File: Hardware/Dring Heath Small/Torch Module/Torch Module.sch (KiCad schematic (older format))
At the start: 32 parts, among them J1 Torch, J2 Module3, J3 Conn_01x18_Male, J4 Limit, J6 Motor, J7 Module1, K1 G6E, Q1 AO3400A, U1 ULN2002

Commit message: Main and Module Boards Routed
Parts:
- removed C3: 1uf, Capacitor_SMD:C_0603_1608Metric_Pad1.08x0.95mm_HandSolder, symbol Device:C_Small
- removed R10: 3.3k, Resistor_SMD:R_0603_1608Metric_Pad0.98x0.95mm_HandSolder, symbol Device:R_US
- removed R8: 10k, Resistor_SMD:R_0603_1608Metric_Pad0.98x0.95mm_HandSolder, symbol Device:R_US
- removed R9: 1k, Resistor_SMD:R_0603_1608Metric_Pad0.98x0.95mm_HandSolder, symbol Device:R_US
- added J10: Module conn, Connector_PinHeader_2.54mm:PinHeader_1x12_P2.54mm_Vertical, symbol Connector:Conn_01x12_Male
- added J8: 2.54 pin, Connector_PinHeader_2.54mm:PinHeader_2x05_P2.54mm_Vertical, symbol Connector:Conn_01x10_Male
- added J9: 1.27 pin, Connector_PinHeader_1.27mm:PinHeader_2x05_P1.27mm_Vertical, symbol Connector:Conn_01x10_Male
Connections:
- net at U1.13 (O4): now also J3.11 (Pin_11)
- net at U1.5 (I5), U1.6 (I6), U1.7 (I7)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: now also J3.15 (Pin_15), J3.9 (Pin_9); no longer U1.4 (I4)
- net at J3.17 (Pin_17): no longer J3.18 (Pin_18)
- net at J3.4 (Pin_4): now also U1.4 (I4)
- new net: J10.1 (Pin_1), J8.3 (Pin_3), J8.5 (Pin_5), J8.9 (Pin_9), J9.3 (Pin_3), J9.5 (Pin_5), J9.9 (Pin_9)
- new net: J10.10 (Pin_10), J8.6 (Pin_6), J9.6 (Pin_6)
- new net: J10.11 (Pin_11), J8.8 (Pin_8), J9.8 (Pin_8)
- new net: J10.3 (Pin_3), J8.1 (Pin_1), J9.1 (Pin_1)
- new net: J10.8 (Pin_8), J8.2 (Pin_2), J9.2 (Pin_2)
- new net: J10.9 (Pin_9), J8.4 (Pin_4), J9.4 (Pin_4)
- no-connect marks 29 -> 37
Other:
- note added: "Jtag"
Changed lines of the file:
@@
 NoConn ~ 3200 3000
 NoConn ~ 3900 3600
-$Comp
-L Transistor_Array:ULN2002 U1
-U 1 1 5FF8EFB7
-P 4100 4950
-F 0 "U1" H 4250 5600 50  0000 C CNN
-F 1 "ULN2002" H 4250 5500 50  0000 C CNN
-F 2 "Package_SO:SO-16_3.9x9.9mm_P1.27mm" H 4150 4400 50  0001 L CNN
-F 3 "http://www.ti.com/lit/ds/symlink/uln2003a.pdf" H 4200 4750 50  0001 C CNN
-	1    4100 4950
-	1    0    0    -1
-$EndComp
-$Comp
-L Device:C_Small C3
-U 1 1 5FF90392
-P 5050 5450
-AR Path="/5FF90392" Ref="C3"  Part="1"
-AR Path="/61469ABE/5FF90392" Ref="C?"  Part="1"
-F 0 "C3" H 4958 5404 50  0000 R CNN
-F 1 "1uf" H 4958 5495 50  0000 R CNN
-F 2 "Capacitor_SMD:C_0603_1608Metric_Pad1.08x0.95mm_HandSolder" H 5050 5450 50  0001 C CNN
-F 3 "~" H 5050 5450 50  0001 C CNN
-	1    5050 5450
-	-1   0    0    1
-$EndComp
-$Comp
-L Device:R_US R8
-U 1 1 5FF9039C
-P 4900 5200
-AR Path="/5FF9039C" Ref="R8"  Part="1"
-AR Path="/61469ABE/5FF9039C" Ref="R?"  Part="1"
-F 0 "R8" V 4700 5300 50  0000 C CNN
-F 1 "10k" V 4800 5250 50  0000 C CNN
-F 2 "Resistor_SMD:R_0603_1608Metric_Pad0.98x0.95mm_HandSolder" V 4940 5190 50  0001 C CNN
-F 3 "~" H 4900 5200 50  0001 C CNN
-	1    4900 5200
-	0    1    1    0
-$EndComp
-$Comp
-L Device:R_US R9
-U 1 1 5FF903A6
-P 4750 5350
-AR Path="/5FF903A6" Ref="R9"  Part="1"
-AR Path="/61469ABE/5FF903A6" Ref="R?"  Part="1"
-F 0 "R9" H 4600 5400 50  0000 L CNN
-F 1 "1k" H 4600 5300 50  0000 L CNN
-F 2 "Resistor_SMD:R_0603_1608Metric_Pad0.98x0.95mm_HandSolder" V 4790 5340 50  0001 C CNN
-F 3 "~" H 4750 5350 50  0001 C CNN
-	1    4750 5350
-	-1   0    0    1
-$EndComp
-$Comp
-L Device:R_US R10
-U 1 1 5FF903B0
-P 4750 5050
-AR Path="/5FF903B0" Ref="R10"  Part="1"
-AR Path="/61469ABE/5FF903B0" Ref="R?"  Part="1"
-F 0 "R10" V 4950 5150 50  0000 R CNN
-F 1 "3.3k" V 4850 5150 50  0000 R CNN
-F 2 "Resistor_SMD:R_0603_1608Metric_Pad0.98x0.95mm_HandSolder" V 4790 5040 50  0001 C CNN
-F 3 "~" H 4750 5050 50  0001 C CNN
-	1    4750 5050
-	-1   0    0    -1
-$EndComp
-Wire Wire Line
-	5050 5350 5050 5200
-Wire Wire Line
-	4100 5550 4750 5550
-Wire Wire Line
-	4750 5550 4750 5500
-Wire Wire Line
-	4750 5550 5050 5550
-Connection ~ 4750 5550
 NoConn ~ 4500 5350
 NoConn ~ 4500 5250
 NoConn ~ 4500 5150
-NoConn ~ 4500 5050
 Wire Wire Line
 	5750 3500 5250 3500
@@
 Wire Wire Line
 	3450 4750 3700 4750
-Connection ~ 4750 5200
 Wire Wire Line
 	4500 4550 4950 4550
@@
 	3600 4850 3700 4850
 Wire Wire Line
-	5050 5200 5050 4150
-Connection ~ 5050 5200
-Wire Wire Line
-	5150 4150 5050 4150
-Connection ~ 5050 4150
-Wire Wire Line
-	4450 4150 4450 4300
-Wire Wire Line
-	4450 4300 4850 4300
-Wire Wire Line
-	4850 4300 4850 4900
-Wire Wire Line
-	4850 4900 4750 4900
-Wire Wire Line
-	3700 5050 3700 5150
-Wire Wire Line
-	3700 5150 3700 5250
-Connection ~ 3700 5150
-Wire Wire Line
-	3700 5250 3700 5350
-Connection ~ 3700 5250
-Wire Wire Line
-	3700 5350 3700 5550
-Wire Wire Line
 	3700 5550 4100 5550
-Connection ~ 3700 5350
-Connection ~ 4100 5550
 Wire Wire Line
 	4500 4950 4550 4950
 Wire Wire Line
 	4550 4950 4550 4150
-NoConn ~ 4850 4150
 NoConn ~ 4350 4150
-NoConn ~ 4250 4150
 NoConn ~ 3950 4150
 NoConn ~ 3850 4150
-NoConn ~ 3750 4150
 NoConn ~ 3650 4150
 NoConn ~ 3550 4150
@@
 	-1   0    0    1
 $EndComp
+$Comp
+L Connector:Conn_01x12_Male J?
+U 1 1 600F49D0
+P 5200 6600
+AR Path="/61469ABE/600F49D0" Ref="J?"  Part="1"
+AR Path="/600F49D0" Ref="J10"  Part="1"
+F 0 "J10" H 5150 7050 50  0000 R CNN
+F 1 "Module conn" V 5100 6700 50  0000 R CNN
+F 2 "Connector_PinHeader_2.54mm:PinHeader_1x12_P2.54mm_Vertical" H 5200 6600 50  0001 C CNN
+F 3 "~" H 5200 6600 50  0001 C CNN
+	1    5200 6600
+	-1   0    0    -1
+$EndComp
+$Comp
+L Connector:Conn_01x10_Male J9
+U 1 1 600FA13A
+P 4000 6600
+F 0 "J9" H 4108 7181 50  0000 C CNN
+F 1 "1.27 pin" H 4108 7090 50  0000 C CNN
+F 2 "Connector_PinHeader_1.27mm:PinHeader_2x05_P1.27mm_Vertical" H 4000 6600 50  0001 C CNN
+F 3 "~" H 4000 6600 50  0001 C CNN
+	1    4000 6600
+	1    0    0    -1
+$EndComp
+$Comp
+L Connector:Conn_01x10_Male J8
+U 1 1 600FD9D8
+P 3450 6600
+F 0 "J8" H 3558 7181 50  0000 C CNN
+F 1 "2.54 pin" H 3558 7090 50  0000 C CNN
+F 2 "Connector_PinHeader_2.54mm:PinHeader_2x05_P2.54mm_Vertical" H 3450 6600 50  0001 C CNN
+F 3 "~" H 3450 6600 50  0001 C CNN
+	1    3450 6600
+	1    0    0    -1
+$EndComp
+Wire Wire Line
+	4200 6300 4750 6300
+Wire Wire Line
+	4750 6300 4750 6800
+Wire Wire Line
+	4750 6800 5000 6800
+Wire Wire Line
+	4200 6500 4700 6500
+Wire Wire Line
+	4700 6500 4700 6900
+Wire Wire Line
+	4700 6900 5000 6900
+Wire Wire Line
+	4200 6700 4650 6700
+Wire Wire Line
+	4650 6700 4650 7000
+Wire Wire Line
+	4650 7000 5000 7000
+Wire Wire Line
+	4200 6900 4600 6900
+Wire Wire Line
+	4600 6900 4600 7100
+Wire Wire Line
+	4600 7100 5000 7100
+Wire Wire Line
+	4850 6300 5000 6300
+Wire Wire Line
+	4200 7000 4400 7000
+Wire Wire Line
+	4400 7000 4400 6600
+Wire Wire Line
+	4200 6600 4400 6600
+Wire Wire Line
+	4200 6200 4850 6200
+Wire Wire Line
+	4850 6200 4850 6300
+Wire Wire Line
+	4200 6400 4400 6400
+Wire Wire Line
+	4400 6400 4400 6600
+Connection ~ 4400 6600
+Wire Wire Line
+	4400 6400 4400 6100
+Wire Wire Line
+	4400 6100 5000 6100
+Connection ~ 4400 6400
+Wire Wire Line
+	3650 6200 3650 6250
+Wire Wire Line
+	3650 6250 4200 6250
+Wire Wire Line
+	4200 6250 4200 6200
+Connection ~ 4200 6200
+Wire Wire Line
+	3650 6300 3650 6350
+Wire Wire Line
+	3650 6350 4200 6350
+Wire Wire Line
+	4200 6350 4200 6300
+Connection ~ 4200 6300
+Wire Wire Line
+	3650 6400 3650 6450
+Wire Wire Line
+	3650 6450 4200 6450
+Wire Wire Line
+	4200 6450 4200 6400
+Connection ~ 4200 6400
+Wire Wire Line
+	3650 6500 3650 6550
+Wire Wire Line
+	3650 6550 4200 6550
+Wire Wire Line
+	4200 6550 4200 6500
+Connection ~ 4200 6500
+Wire Wire Line
+	3650 6600 3650 6650
+Wire Wire Line
+	3650 6650 4200 6650
+Wire Wire Line
+	4200 6650 4200 6600
+Connection ~ 4200 6600
+Wire Wire Line
+	3650 6700 3650 6750
+Wire Wire Line
+	3650 6900 3650 6950
+Wire Wire Line
+	3650 6950 4200 6950
+Wire Wire Line
+	4200 6950 4200 6900
+Connection ~ 4200 6900
+Wire Wire Line
+	3650 7000 3650 7050
+Wire Wire Line
+	3650 7050 4200 7050
+Wire Wire Line
+	4200 7050 4200 7000
+Connection ~ 4200 7000
+Wire Notes Line
+	3300 5900 5500 5900
+Wire Notes Line
+	5500 5900 5500 7450
+Wire Notes Line
+	5500 7450 3300 7450
+Wire Notes Line
+	3300 7450 3300 5900
+Text Notes 3400 7400 0    118  ~ 24
+Jtag
+NoConn ~ 5000 6200
+NoConn ~ 5000 6400
+NoConn ~ 5000 6500
+NoConn ~ 5000 6600
+NoConn ~ 5000 6700
+NoConn ~ 5000 7200
+Wire Wire Line
+	3650 6750 4200 6750
+Wire Wire Line
+	4200 6750 4200 6700
+Connection ~ 4200 6700
+NoConn ~ 3650 6800
+NoConn ~ 3650 7100
+NoConn ~ 4200 7100
+NoConn ~ 4200 6800
+NoConn ~ 5150 4150
+NoConn ~ 5050 4150
+Wire Wire Line
+	3750 4150 3750 4250
+Wire Wire Line
+	3750 4250 3500 4250
+Wire Wire Line
+	3500 4250 3500 5050
+Wire Wire Line
+	3500 5050 3700 5050
+Wire Wire Line
+	3700 5350 3700 5550
+Connection ~ 3700 5350
+Wire Wire Line
+	3700 5250 3700 5350
+Wire Wire Line
+	3700 5150 3700 5250
+Connection ~ 3700 5250
+$Comp
+L Transistor_Array:ULN2002 U1
+U 1 1 5FF8EFB7
+P 4100 4950
+F 0 "U1" H 4250 5600 50  0000 C CNN
+F 1 "ULN2002" H 4250 5500 50  0000 C CNN
+F 2 "Package_SO:SO-16_3.9x9.9mm_P1.27mm" H 4150 4400 50  0001 L CNN
+F 3 "http://www.ti.com/lit/ds/symlink/uln2003a.pdf" H 4200 4750 50  0001 C CNN
+	1    4100 4950
+	1    0    0    -1
+$EndComp
+Wire Wire Line
+	4500 5050 4850 5050
+Wire Wire Line
+	4850 5050 4850 4300
+Wire Wire Line
+	4850 4300 4450 4300
+Wire Wire Line
+	4450 4300 4450 4150
+Wire Wire Line
+	4250 4150 4250 4200
+Wire Wire Line
+	4250 4200 4850 4200
+Wire Wire Line
+	4850 4200 4850 4150
+Wire Wire Line
+	4850 4200 5000 4200
+Wire Wire Line
+	5000 4200 5000 5550
+Wire Wire Line
+	5000 5550 4100 5550
+Connection ~ 4850 4200
+Connection ~ 4100 5550
 $EndSCHEMATC

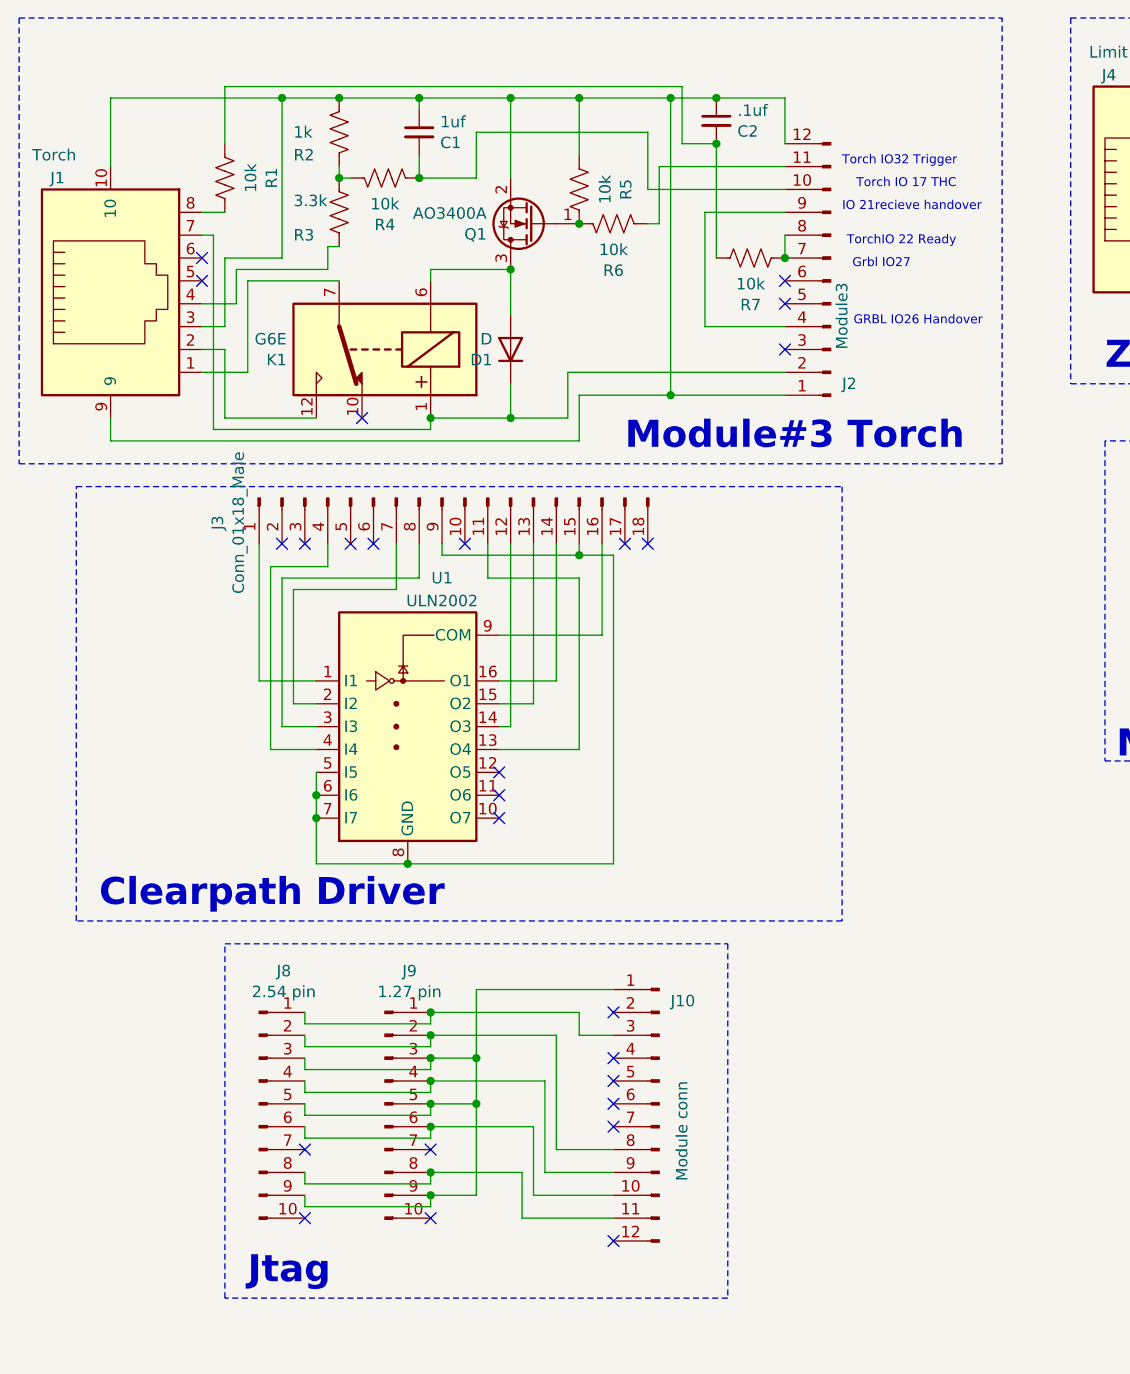
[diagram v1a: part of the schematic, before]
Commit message: Pin changes
Put RJ45 connector on Jtag module for more IO put Pot on Torch module to
adjust Plasma voltage
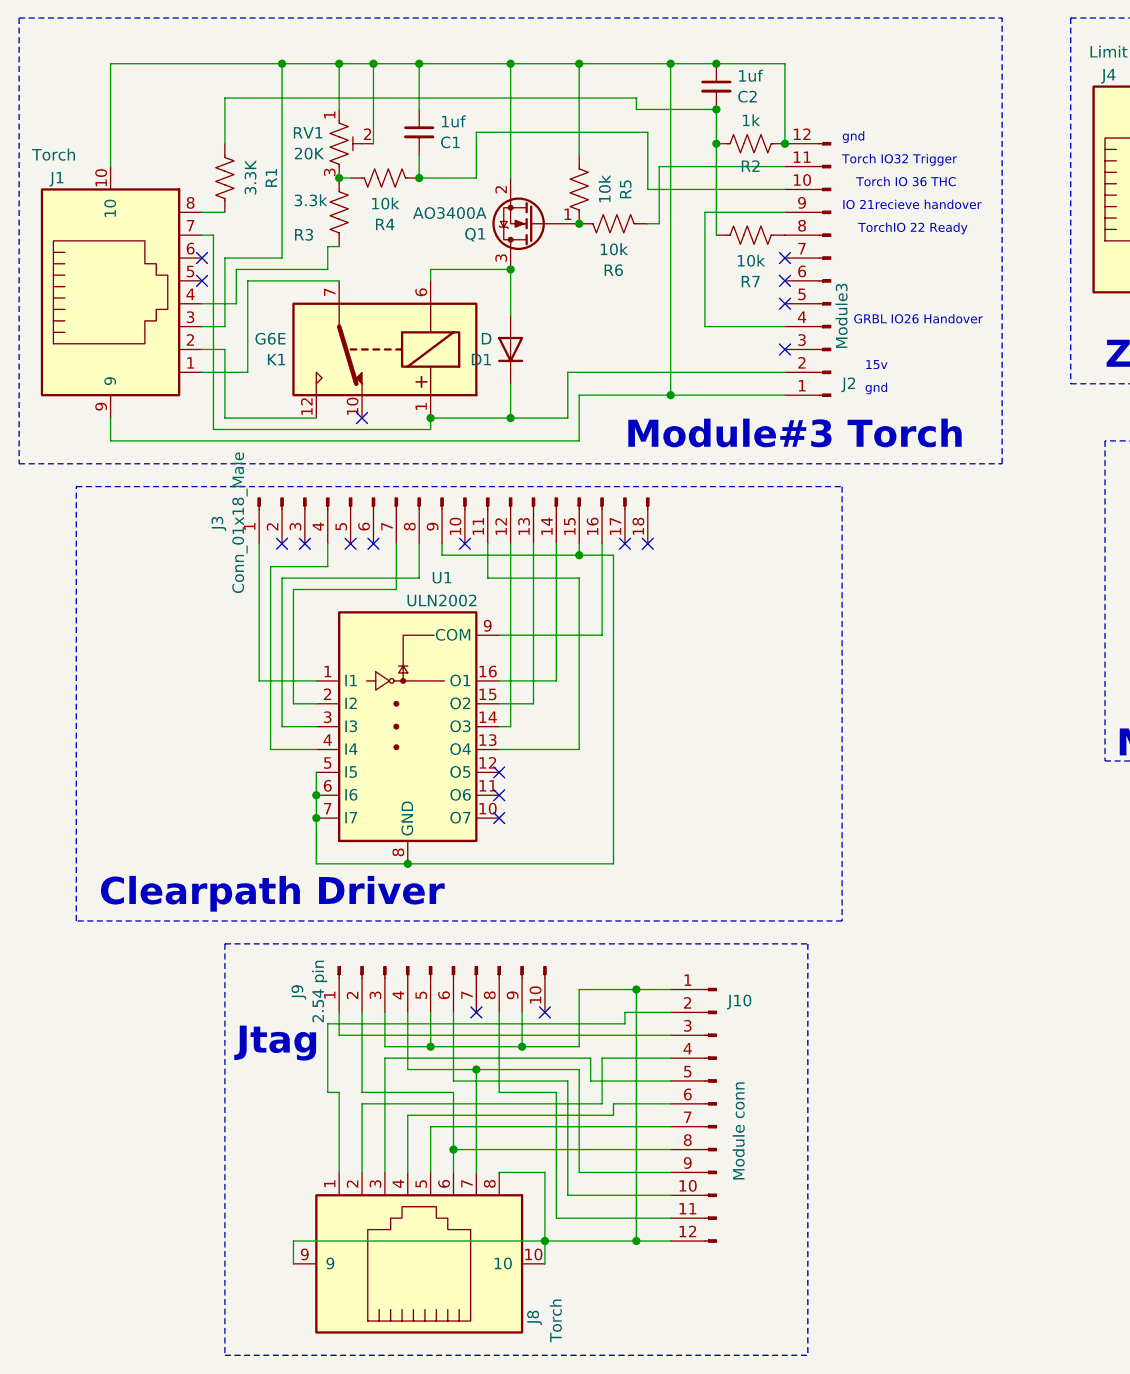
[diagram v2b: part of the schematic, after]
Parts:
- removed J8: 2.54 pin, Connector_PinHeader_2.54mm:PinHeader_2x05_P2.54mm_Vertical, symbol Connector:Conn_01x10_Male
- added J8: Torch, Modules:RJ45_Torb_Vertical, symbol My_library:8P8C_Shielded
- added RV1: 20K, Potentiometer_THT:Potentiometer_Bourns_3339S_Horizontal, symbol Device:R_POT_TRIM_US
- C2: value .1uf -> 1uf
- J9: value 1.27 pin -> 2.54 pin; footprint Connector_PinHeader_1.27mm:PinHeader_2x05_P1.27mm_Vertical -> Connector_PinHeader_2.54mm:PinHeader_2x05_P2.54mm_Vertical
- R1: value 10k -> 3.3K
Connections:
- net at C1.1, C2.1, J1.10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: now also RV1.1, RV1.2
- net at J10.1 (Pin_1), J9.3 (Pin_3), J9.5 (Pin_5)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: now also J10.12 (Pin_12), J8.10, J8.8, J8.9
- net at J10.2 (Pin_2): now also J8.1
- net at J10.4 (Pin_4): now also J8.2
- net at J10.5 (Pin_5): now also J8.3
- net at J10.6 (Pin_6): now also J8.4
- net at J10.7 (Pin_7): now also J8.5
- net at J10.8 (Pin_8), J9.2 (Pin_2): now also J8.6
- net at J10.9 (Pin_9), J9.4 (Pin_4): now also J8.7
- net at R3.2, R4.2: now also RV1.3; no longer R2.1
- net at J2.8 (Pin_8), R7.2: no longer J2.7 (Pin_7)
- net at C2.2, R1.2, R7.1: now also R2.1
- no-connect marks 37 -> 30
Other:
- note added: "15v"
- note added: "Torch IO 36 THC"
- note added: "gnd"
- note removed: "Grbl IO27"
- note removed: "Torch IO 17 THC"
- moved on the sheet: C2, J10, J9
